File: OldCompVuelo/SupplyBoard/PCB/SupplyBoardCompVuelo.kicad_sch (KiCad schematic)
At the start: 3 parts, among them J1 XT60-M, J2 NebulaConnector, SW1 SW_SPDT

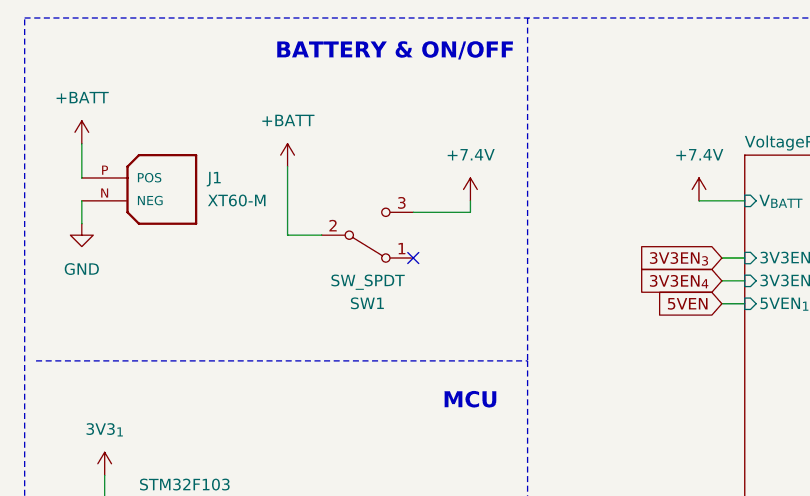
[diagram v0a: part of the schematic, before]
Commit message: start a new version of the flight computer
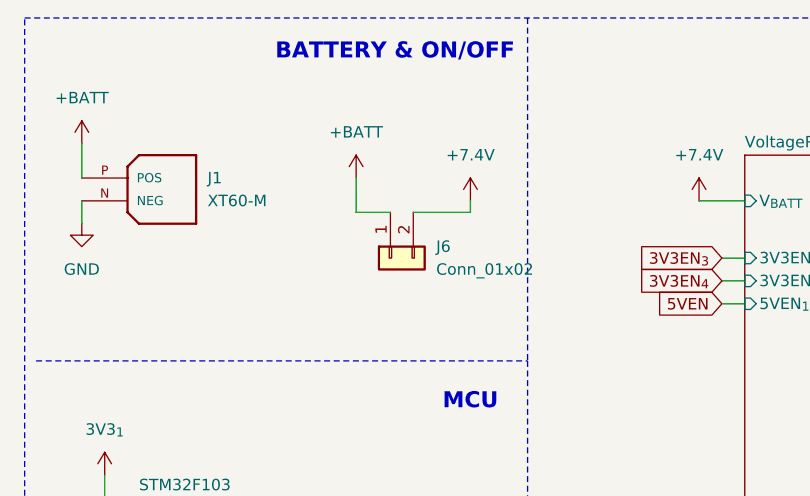
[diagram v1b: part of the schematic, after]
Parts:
- removed SW1: SW_SPDT, CompVuelo:SWSPDT, symbol CompVuelo:SW_SPDT
- added J6: Conn_01x02, symbol Connector_Generic:Conn_01x02
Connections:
- net +7.4V: now also J6.2 (Pin_2)
- net +BATT: now also J6.1 (Pin_1)
- no-connect marks 1 -> 0
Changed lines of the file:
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@@
 		)
-	)
-	(no_connect
-		(at 58.42 41.91)
 	)
 	(polyline
@@
 	(wire
 		(pts
-			(xy 44.45 39.37) (xy 48.26 39.37)
+			(xy 52.07 36.83) (xy 55.88 36.83)
 		)
 		(stroke
@@
 			(width 0)
 			(type dash)
+		)
+	)
+	(wire
+		(pts
+			(xy 52.07 33.02) (xy 52.07 36.83)
+		)
+		(stroke
+			(width 0)
+			(type default)
 		)
 	)
@@
 		(pts
 			(xy 62.23 110.49) (xy 62.23 116.84)
-		)
-		(stroke
-			(width 0)
-			(type default)
-		)
-	)
-	(wire
-		(pts
-			(xy 44.45 31.75) (xy 44.45 39.37)
 		)
 		(stroke
@@
 	)
 	(symbol
-		(lib_id "CompVuelo:SW_SPDT")
-		(at 53.34 44.45 0)
-		(mirror x)
-		(unit 1)
-		(exclude_from_sim no)
-		(in_bom yes)
-		(on_board yes)
-		(dnp no)
-		(property "Reference" "SW1"
-			(at 53.34 46.99 0)
-			(effects
-				(font
-					(size 1.27 1.27)
-				)
-			)
-		)
-		(property "Value" "SW_SPDT"
-			(at 53.34 44.45 0)
-			(effects
-				(font
-					(size 1.27 1.27)
-				)
-			)
-		)
-		(property "Footprint" "CompVuelo:SWSPDT"
-			(at 53.34 44.45 0)
-			(effects
-				(font
-					(size 1.27 1.27)
-				)
-				(hide yes)
-			)
-		)
-		(property "Datasheet" "https://www.lcsc.com/datasheet/C19189120.pdf"
-			(at 53.34 44.45 0)
-			(effects
-				(font
-					(size 1.27 1.27)
-				)
-				(hide yes)
-			)
-		)
-		(property "Description" ""
-			(at 53.34 44.45 0)
-			(effects
-				(font
-					(size 1.27 1.27)
-				)
-				(hide yes)
-			)
-		)
-		(pin "1"
-		)
-		(pin "2"
-		)
-		(pin "3"
-		)
-		(instances
-			(project ""
-				(path "/2119c5ce-afa8-4b00-8fd4-fc653d4beb45"
-					(reference "SW1")
-					(unit 1)
-				)
-			)
-		)
-	)
-	(symbol
 		(lib_id "power:+7.5V")
 		(at 139.7 31.75 0)
@@
 	)
 	(symbol
+		(lib_id "Connector_Generic:Conn_01x02")
+		(at 55.88 41.91 90)
+		(mirror x)
+		(unit 1)
+		(exclude_from_sim no)
+		(in_bom yes)
+		(on_board yes)
+		(dnp no)
+		(fields_autoplaced yes)
+		(property "Reference" "J6"
+			(at 60.96 40.6399 90)
+			(effects
+				(font
+					(size 1.27 1.27)
+				)
+				(justify right)
+			)
+		)
+		(property "Value" "Conn_01x02"
+			(at 60.96 43.1799 90)
+			(effects
+				(font
+					(size 1.27 1.27)
+				)
+				(justify right)
+			)
+		)
+		(property "Footprint" ""
+			(at 55.88 41.91 0)
+			(effects
+				(font
+					(size 1.27 1.27)
+				)
+				(hide yes)
+			)
+		)
+		(property "Datasheet" "~"
+			(at 55.88 41.91 0)
+			(effects
+				(font
+					(size 1.27 1.27)
+				)
+				(hide yes)
+			)
+		)
+		(property "Description" "Generic connector, single row, 01x02, script generated (kicad-library-utils/schlib/autogen/connector/)"
+			(at 55.88 41.91 0)
+			(effects
+				(font
+					(size 1.27 1.27)
+				)
+				(hide yes)
+			)
+		)
+		(pin "1"
+		)
+		(pin "2"
+		)
+		(instances
+			(project ""
+				(path "/2119c5ce-afa8-4b00-8fd4-fc653d4beb45"
+					(reference "J6")
+					(unit 1)
+				)
+			)
+		)
+	)
+	(symbol
 		(lib_id "power:+BATT")
 		(at 21.59 29.21 0)
@@
 	(symbol
 		(lib_id "power:+BATT")
-		(at 44.45 31.75 0)
+		(at 52.07 33.02 0)
 		(unit 1)
 		(exclude_from_sim no)
@@
 		(fields_autoplaced yes)
 		(property "Reference" "#PWR05"
-			(at 44.45 35.56 0)
+			(at 52.07 36.83 0)
 			(effects
 				(font
@@
 		)
 		(property "Value" "+BATT"
-			(at 44.45 26.67 0)
+			(at 52.07 27.94 0)
 			(effects
 				(font
@@
 		)
 		(property "Footprint" ""
-			(at 44.45 31.75 0)
+			(at 52.07 33.02 0)
 			(effects
 				(font
@@
 		)
 		(property "Datasheet" ""
-			(at 44.45 31.75 0)
+			(at 52.07 33.02 0)
 			(effects
 				(font
@@
 		)
 		(property "Description" "Power symbol creates a global label with name \"+BATT\""
-			(at 44.45 31.75 0)
-			(effects
-				(font
+			(at 52.07 33.02 0)
+			(effects
+				(font
